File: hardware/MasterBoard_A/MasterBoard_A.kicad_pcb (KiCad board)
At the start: 2 copper layers, 60 x 100 mm, 175 parts, among them J101 Main Current Hall Sensor, J102 Global LV and CAN, J103 HRLV, J105 Conn_02x05_Odd_Even, J106 uart, J301 RJ45_Amphenol_RJMG1BD3B8K1ANR, K101 G5Q-1A 24Vdc, Q101 MMBT5550L, Q102 MMBT5550L, Q103 MMBT5550L, Q301 MMBT5550L, Q302 MMBT5550L, Q401 MMBT5550L, Q501 MMBT5550L, Q502 MMBT5550L, SW101 SW_Push, U101 MCP2542FDxMF, U102 MCP2542FDxMF, U104 MCP9700x-ETT, U105 XM0G3507QPTRQ1, U201 Si1450DH, U202 LM74502, U203 Si1450DH, U204 AP64060ZQ, U205 AP64060ZQ, U301 W5500, U401 MCP1501-40xSN, U402 TLV713185PDBV, U403 NSI5030, U404 MCP33151, U405 MCP33151, U406 MIC7300M5, U407 Si1450DH, U408 Si1450DH, U409 NCV68061, U501 NSI5030, U502 Si1450DH, U503 NCV68061, U504 MCP2542FDxMF, U505 AP7384-50SA, U506 ISOM8110, U507 ISOM8110, U508 STISO620, Y301 Crystal_GND24

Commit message: bucks and eyeballed layout
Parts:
- added C321: 220n, Capacitor_SMD:C_0805_2012Metric_Pad1.18x1.45mm_HandSolder, F.Cu at (136.6, 106.9)
- moved R209 69.5 mm to (176.3, 135.5), turned to 180 degrees
- moved R201 60.9 mm to (172.8, 120.9), turned to -90 degrees
- moved U204 60.7 mm to (179.1, 121.8), turned to 180 degrees
- moved C205 58.1 mm to (176.3, 130.7)
- moved C206 57.1 mm to (176.3, 133.0)
- moved C204 54.8 mm to (179.5, 124.8), turned to 180 degrees
- moved D203 54.5 mm to (180.6, 127.8)
- moved C207 53.7 mm to (180.9, 134.1), turned to 90 degrees
- moved R207 53.5 mm to (183.0, 134.2), turned to -90 degrees
- moved C203 51.9 mm to (179.6, 118.5)
- moved L201 47.7 mm to (175.4, 126.3), turned to 90 degrees
- moved D201 43.1 mm to (174.9, 121.5), turned to 90 degrees
- moved R208 38.9 mm to (183.2, 121.7), turned to -90 degrees
- moved R204 36.8 mm to (173.1, 101.0), turned to -90 degrees
- moved D202 33.9 mm to (175.1, 101.0), turned to 90 degrees
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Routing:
- net +3.3V: track 0.00 -> 95.5 mm, vias 0 -> 1
- net +5V: track 0.00 -> 25.2 mm
- net Net-(U204-FB): track 0.00 -> 15.9 mm
- net Net-(U205-FB): track 0.00 -> 15.6 mm
- net Net-(D203-K): track 0.00 -> 7.65 mm
- net Net-(D204-K): track 0.00 -> 7.38 mm
- net LV+: track 27.5 -> 33.4 mm
- net Net-(C213-Pad1): track 0.00 -> 3.35 mm
- net Net-(C207-Pad1): track 0.00 -> 3.19 mm
- net GND: track 18.0 -> 21.0 mm, vias 53 -> 72
- net Net-(D201-A): track 0.00 -> 2.57 mm
- net Net-(U205-BST): track 0.00 -> 2.25 mm
- net Net-(U204-BST): track 0.00 -> 2.14 mm
- net Net-(D202-A): track 0.00 -> 2.01 mm

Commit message: saturn tool kit my beloved
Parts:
- moved C506 58.6 mm to (188.2, 133.4), turned to 90 degrees
- moved U508 49.7 mm to (184.2, 141.0), turned to -90 degrees
- moved U502 45.9 mm to (150.0, 152.0), turned to 90 degrees
- moved Q501 45.4 mm to (137.0, 147.0), turned to -22.5 degrees
- moved U504 45.3 mm to (173.5, 149.1), turned to 180 degrees
- moved R506 44.2 mm to (142.6, 148.4), turned to -45 degrees
- moved R504 43.9 mm to (172.0, 152.8), turned to 180 degrees
- moved Q502 43.0 mm to (147.2, 147.6), turned to 180 degrees
- moved U506 42.4 mm to (133.0, 141.0)
- moved R505 42.1 mm to (168.4, 155.6), turned to 90 degrees
- moved R503 41.6 mm to (140.6, 145.4), turned to 180 degrees
- moved C505 40.9 mm to (179.2, 146.4), turned to -90 degrees
- moved U505 40.6 mm to (144.2, 156.8), turned to -90 degrees
- moved C501 40.5 mm to (151.2, 145.4), turned to 180 degrees
- moved C503 40.2 mm to (145.4, 152.0), turned to -90 degrees
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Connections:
- J103 pad 1: /HRLV_CAN- -> /HRLV_CAN+
- J103 pad 4: /HRLV_CAN+ -> /HRLV_CAN-
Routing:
- net /HRLV interface/+5V: track 0.00 -> 68.0 mm
- net +3.3V: track 95.5 -> 153.9 mm, vias 1 -> 5
- net /HRLV interface/LV+: track 0.00 -> 54.7 mm
- net /HRLV_LV+: track 0.00 -> 21.4 mm
- net Net-(U504-RXD): track 0.00 -> 10.8 mm
- net Net-(U504-TXD): track 0.00 -> 10.4 mm
- net /HRLV_IL+: track 0.00 -> 9.38 mm
- net /HRLV_CAN-: track 0.00 -> 9.17 mm
- net /HRLV_CAN+: track 0.00 -> 9.17 mm
- net Net-(D503-K): track 0.00 -> 7.49 mm
- net /HRLV_IL-: track 0.00 -> 6.94 mm
- net Net-(Q502-E): track 0.00 -> 5.89 mm
- net Net-(U506--TX): track 0.00 -> 5.83 mm
- net Net-(U502-G): track 0.00 -> 5.23 mm
- net Net-(U507--TX): track 0.00 -> 5.08 mm, vias 0 -> 2
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- added copper zone on B.Cu, net /HRLV_LV-
- added copper zone on F.Cu, net /HRLV_LV-

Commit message: mb layout: all but mcu bundle
thou who completes thy layout must endure excel
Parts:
- removed C103, C405, C407: 220n, Capacitor_SMD:C_0805_2012Metric_Pad1.18x1.45mm_HandSolder
- removed D401: 10V, Diode_SMD:D_0805_2012Metric_Pad1.15x1.40mm_HandSolder
- removed Q401: MMBT5550L, Package_TO_SOT_SMD:SOT-23
- removed R101, R103, R401, R504: 40.2k, Resistor_SMD:R_0805_2012Metric_Pad1.20x1.40mm_HandSolder
- removed R402, R403: 22.1k, Resistor_SMD:R_0805_2012Metric_Pad1.20x1.40mm_HandSolder
- removed U403: NSI5030, Diode_SMD:Nexperia_CFP3_SOD-123W
- removed U406: MIC7300M5, Package_TO_SOT_SMD:TSOT-23-5
- removed U407: Si1450DH, Package_TO_SOT_SMD:SOT-363_SC-70-6_Handsoldering
- moved U401 52.3 mm to (154.7, 124.8), turned to 180 degrees
- moved C401 43.9 mm to (156.6, 130.6), turned to 180 degrees
- moved C402 43.0 mm to (156.6, 128.6), turned to 180 degrees
- moved U402 42.6 mm to (156.7, 133.4), turned to 180 degrees
- moved U408 41.9 mm to (142.4, 133.3)
- moved U409 35.9 mm to (148.2, 133.3), turned to 180 degrees
- moved C406 35.4 mm to (152.7, 130.2), turned to -90 degrees
- moved U101 34.4 mm to (181.2, 120.2)
- moved J101 34.1 mm to (138.1, 130.0), turned to 90 degrees
- moved U405 32.7 mm to (147.6, 122.0), turned to 90 degrees
- moved U104 32.5 mm to (207.5, 96.4)
- moved C408 29.5 mm to (148.1, 130.0)
- moved C409 29.3 mm to (148.1, 127.0)
- moved U102 29.0 mm to (186.6, 127.1), turned to 90 degrees
- moved C404 28.7 mm to (141.3, 120.2), turned to 90 degrees
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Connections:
- C410 pad 1: /Main Current Hall Sensing/Vreg -> +5V
- J102 pad 3: /G_CAN_+ -> /G_CAN-
- J102 pad 6: /G_CAN_- -> /G_CAN+
- U101 pad 8: Net-(U101-STBY) -> GND
- U102 pad 8: Net-(U102-STBY) -> GND
- U402 pad 3: Net-(U402-EN) -> +5V
- U408 pad 4: /Main Current Hall Sensing/Vreg -> +5V
- U409 pad 3: /Main Current Hall Sensing/Vreg -> +5V
- U409 pad 6: /Main Current Hall Sensing/Vreg -> +5V
- U504 pad 8: Net-(U504-STBY) -> /HRLV_LV-
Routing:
- net +5V: track 25.2 -> 123.7 mm
- net /G_CAN+: track 0.00 -> 67.4 mm, vias 0 -> 2
- net /G_CAN-: track 0.00 -> 67.4 mm, vias 0 -> 2
- net LV+: track 33.4 -> 80.2 mm
- net +3.3V: track 153.9 -> 191.5 mm
- net /Main Current Hall Sensing/4.096Vref: track 0.00 -> 25.3 mm
- net /Main Current Hall Sensing/1.8VA: track 0.00 -> 23.6 mm, vias 0 -> 2
- net /MCHall_5Vin: track 0.00 -> 12.7 mm
- net /HRLV interface/CAN_RX: track 0.00 -> 10.9 mm
- net Net-(U404-Ain+): track 0.00 -> 10.2 mm
- net /HRLV interface/CAN_TX: track 0.00 -> 8.19 mm
- net /mchs.MISO/POCI: track 0.00 -> 6.89 mm
- net Net-(U408-G): track 0.00 -> 6.30 mm, vias 0 -> 2
- net /mchs.SCLK: track 0.00 -> 5.99 mm, vias 0 -> 2
- net Net-(U405-Ain+): track 0.00 -> 4.87 mm
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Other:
- board text added: "trust me bro, length tuning can to mm match is essential"

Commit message: mb ready for review
one of yall poor souls has to verify the schematic and layout
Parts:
- removed C106: 220n, Capacitor_SMD:C_0805_2012Metric_Pad1.18x1.45mm_HandSolder
- removed SW101: SW_Push, Button_Switch_SMD:SW_SPST_PTS645
- removed TP101: TestPoint, TestPoint:TestPoint_THTPad_3.0x3.0mm_Drill1.5mm
- removed TP102, TP103, TP104: TestPoint, TestPoint:TestPoint_Loop_D2.50mm_Drill1.0mm_LowProfile
- removed U104: MCP9700x-ETT, Package_TO_SOT_SMD:SOT-23-3
- added C208: 220n, Capacitor_SMD:C_0805_2012Metric_Pad1.18x1.45mm_HandSolder, F.Cu at (156.9, 136.8)
- added R1: 100, Resistor_SMD:R_1206_3216Metric_Pad1.30x1.75mm_HandSolder, F.Cu at (145.7, 114.6)
- added R2: 100, Resistor_SMD:R_1206_3216Metric_Pad1.30x1.75mm_HandSolder, F.Cu at (147.9, 114.6)
- added R311: 4.99k, Resistor_SMD:R_1206_3216Metric_Pad1.30x1.75mm_HandSolder, F.Cu at (134.9, 110.3)
- added R312: 4.99k, Resistor_SMD:R_1206_3216Metric_Pad1.30x1.75mm_HandSolder, F.Cu at (134.9, 112.6)
- C313: value 100n -> 220n; footprint Capacitor_SMD:C_0603_1608Metric_Pad1.08x0.95mm_HandSolder -> Capacitor_SMD:C_0805_2012Metric_Pad1.18x1.45mm_HandSolder
- moved J106 86.0 mm to (135.4, 121.0), turned to 180 degrees
- moved C107 84.7 mm to (143.3, 114.6), turned to -90 degrees
- moved J105 79.1 mm to (152.8, 110.5), turned to -90 degrees
- moved R111 61.2 mm to (172.2, 108.5), turned to 180 degrees
- moved U105 56.1 mm to (162.7, 110.0), turned to 180 degrees
- moved D106 54.3 mm to (168.8, 120.4), turned to 180 degrees
- moved D104 53.7 mm to (168.8, 118.5), turned to 180 degrees
- moved D103 53.7 mm to (173.4, 98.8), turned to -90 degrees
- moved D105 53.7 mm to (172.8, 106.4)
- moved R109 42.6 mm to (172.8, 104.5), turned to 180 degrees
- moved C321 42.3 mm to (155.4, 69.0)
- moved R112 41.2 mm to (172.7, 112.6)
- moved R107 40.0 mm to (172.8, 102.6), turned to 180 degrees
- moved C109 37.2 mm to (172.7, 110.7)
- moved C110 36.6 mm to (172.7, 114.6)
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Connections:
- net Net-(U105-VCORE) renamed /vcore
- C313 pad 1: /Ethernet/+3.3VA -> +3.3V
- D103 pad 1: Net-(D103-K) -> GND
- D103 pad 2: /led.i2 -> Net-(D103-A)
- D105 pad 1: Net-(D105-K) -> GND
- D105 pad 2: /led.BMSFault -> Net-(D105-A)
- R107 pad 1: Net-(D103-K) -> Net-(D103-A)
- R107 pad 2: GND -> /led.i2
- R109 pad 1: Net-(D105-K) -> Net-(D105-A)
- R109 pad 2: GND -> /led.BMSFault
- U105 pad 11: unconnected-(U105-PA5_HFXIN_FCC_IN-Pad11) -> /led.BMSFault
- U105 pad 12: unconnected-(U105-PA6_HFCLK_IN_HFXOUT-Pad12) -> /led.i2
- U105 pad 21: unconnected-(U105-PB7-Pad21) -> /IL.sense
- U105 pad 22: unconnected-(U105-PB8-Pad22) -> /IL.forward
- U105 pad 23: unconnected-(U105-PB9-Pad23) -> GND
- U105 pad 24: unconnected-(U105-PB14-Pad24) -> /eth.reset_N
- U105 pad 25: unconnected-(U105-PB15-Pad25) -> /eth.irq_N
- U105 pad 27: unconnected-(U105-PA12_FCC_IN-Pad27) -> /eth.SCLK
- U105 pad 28: unconnected-(U105-PA13-Pad28) -> /eth.MISO/POCI
- U105 pad 29: unconnected-(U105-PA14_CLK_OUT_A0_12-Pad29) -> /eth.MOSI/PICO
- U105 pad 30: unconnected-(U105-PA15_A1_0-Pad30) -> /eth.cs_N
- U105 pad 31: unconnected-(U105-PA16_A1_1_FCC_IN-Pad31) -> /mchs.MISO/POCI
- U105 pad 32: unconnected-(U105-PA17_A1_2-Pad32) -> /mchs.SCLK
- U105 pad 33: unconnected-(U105-PA18_A1_3-Pad33) -> /mchs.MOSI/PICO
- U105 pad 34: unconnected-(U105-PA19_SWDIO-Pad34) -> /prog.SWDIO
- U105 pad 35: unconnected-(U105-PA20_SWCLK-Pad35) -> /prog.SWCLK
- U105 pad 36: unconnected-(U105-PB17_A1_4-Pad36) -> +3.3V
- U105 pad 37: unconnected-(U105-PB18_A1_5-Pad37) -> /mchs.cs_per
- U105 pad 38: unconnected-(U105-PB19_A1_6-Pad38) -> /mchs.cs_imp
- U105 pad 39: unconnected-(U105-PA21_A1_7_VREF--Pad39) -> /prog.uart_ui_tx
- U105 pad 40: unconnected-(U105-PA22_CLK_OUT_A0_7-Pad40) -> /prog.uart_ui_rx
- U105 pad 41: unconnected-(U105-PB20_A0_6-Pad41) -> /hrlv.pres_hrlv
- U105 pad 42: unconnected-(U105-PB24_A0_5-Pad42) -> /hrlv.pres_interlock
- U105 pad 43: unconnected-(U105-PA23_VREF+-Pad43) -> /led.sched
- U105 pad 44: unconnected-(U105-PA24_A0_3-Pad44) -> /led.i1
- U105 pad 46: unconnected-(U105-PA26_A0_1-Pad46) -> /can.tx
- U105 pad 47: unconnected-(U105-PA27_RTC_OUT_A0_0-Pad47) -> /can.rx
- U105 pad 5: unconnected-(U105-PA31_CLK_OUT-Pad5) -> +3.3V
- U301 pad 25: Net-(Q301-B) -> Net-(U301-LINKLED)
- U301 pad 27: Net-(Q302-B) -> Net-(U301-ACTLED)
- U404 pad 7: /mchs.MISO/POCI -> /Main Current Hall Sensing/SDO
- U404 pad 8: /mchs.SCLK -> /Main Current Hall Sensing/SCLK
- U405 pad 7: /mchs.MISO/POCI -> /Main Current Hall Sensing/SDO
- U405 pad 8: /mchs.SCLK -> /Main Current Hall Sensing/SCLK
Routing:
- net +3.3V: track 191.5 -> 299.9 mm, vias 5 -> 8
- net /hrlv.pres_hrlv: track 0.00 -> 48.1 mm, vias 0 -> 2
- net /IL.forward: track 0.00 -> 47.6 mm
- net /hrlv.pres_interlock: track 1.20 -> 37.3 mm, vias 0 -> 2
- net /prog.uart_ui_rx: track 0.00 -> 28.9 mm, vias 0 -> 2
- net /prog.uart_ui_tx: track 0.00 -> 27.9 mm, vias 0 -> 2
- net /can.rx: track 0.00 -> 23.0 mm
- net /eth.MOSI/PICO: track 0.00 -> 20.2 mm, vias 0 -> 2
- net /Main Current Hall Sensing/SCLK: track 0.00 -> 19.4 mm
- net /mchs.cs_per: track 0.00 -> 19.3 mm, vias 0 -> 2
- net /mchs.cs_imp: track 0.00 -> 18.7 mm, vias 0 -> 2
- net /eth.cs_N: track 0.00 -> 18.5 mm
- net Net-(Q301-B): track 45.3 -> 26.9 mm
- net /eth.MISO/POCI: track 0.00 -> 18.2 mm, vias 0 -> 2
- net /eth.SCLK: track 0.00 -> 17.5 mm
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- added copper zone on F.Cu, net +3.3V
- added copper zone on F.Cu, net /vcore
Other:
- outline, holes or cut-outs redrawn
- board text added: "100MB/S ethernet"
- board text added: "5V out"
- board text added: "Big Hall Sensor"
- board text added: "CAN+"
- board text added: "CAN-"
- board text added: "GLV+ (9,34)V"
- board text added: "GLV-"
- board text added: "GND"
- board text added: "HRLV interface"
- board text added: "IL return"
- board text added: "IL_A"
- board text added: "IL_B"
- board text added: "LV+ (5.5 , 35)V"
- board text added: "LV-"
- board text added: "Master Board A 1.1 (testing use only) github.com/Gregification/BeeMS/ 1/13/2025 - pinning & hardware info: {dblquote}/hardware/MasterBoard_A/meta.xlsx{dblquote} - software: {dblquote}/MB_MSPM0G3507_A{dblquote} - no hardware watchdog - no PWM bank"
- board text added: "RX"
- board text added: "TX"
- board text added: "bms fault"
- board text added: "impercise"
- board text added: "indicator 1"
- board text added: "indicator 2"
- board text added: "percise"
- board text added: "scheduler"
- board text added: "tty 115200 8N1"
- board text added: "we dont talk about this routing"
- board text removed: "CAN bus"
- board text removed: "JLCJLCJLCJLC"
- board text removed: "Master Board A 1.0 (testing use only) github.com/Gregification/BeeMS/ 12/24/2025 - pinning & hardware info: {dblquote}/hardware/MasterBoard_A/meta.xlsx{dblquote} - software: {dblquote}/MB_MSPM0G3507_A{dblquote} - no hardware watchdog - reduced pwm bank. POC."
- board text removed: "TSBP internal LV interface"
- board text removed: "ethernet"
- board text removed: "fuse >0.4A"
- board text removed: "fuse >0.8A"
- board text removed: "interlock"
- board text removed: "pwm bank 1"

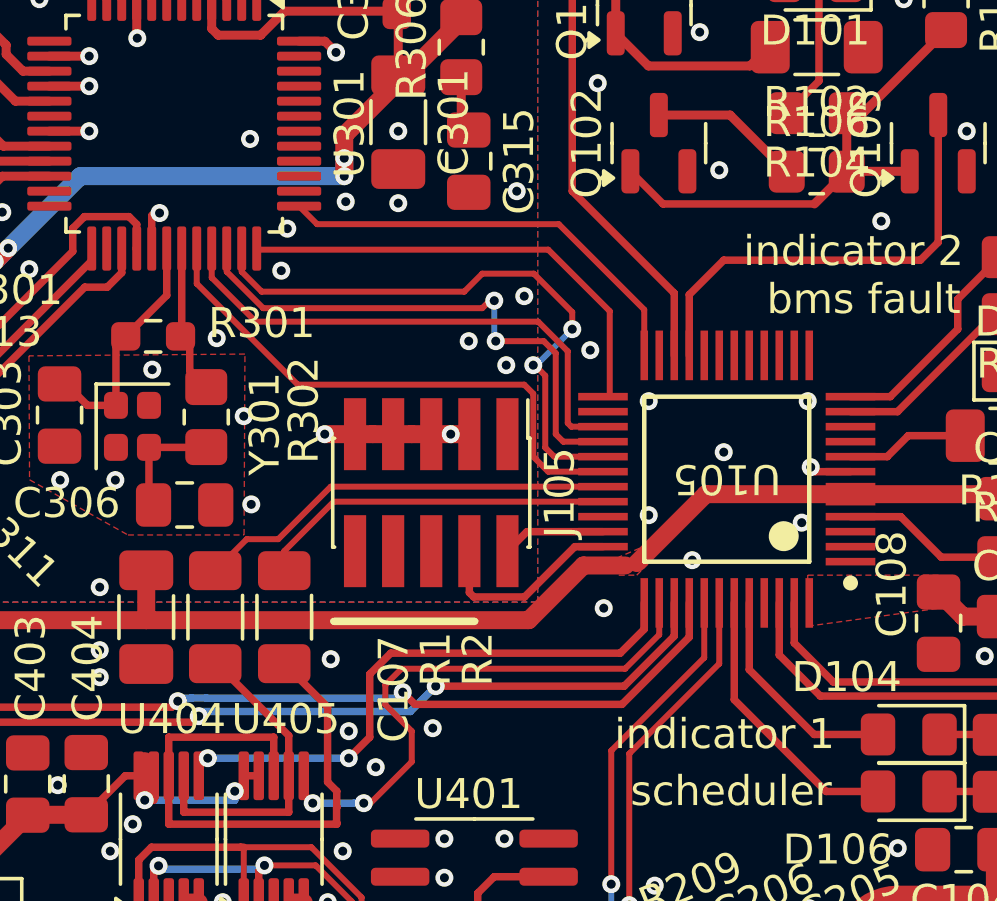
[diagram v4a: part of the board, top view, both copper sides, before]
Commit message: master board shuffling
jlc says $2. yippie
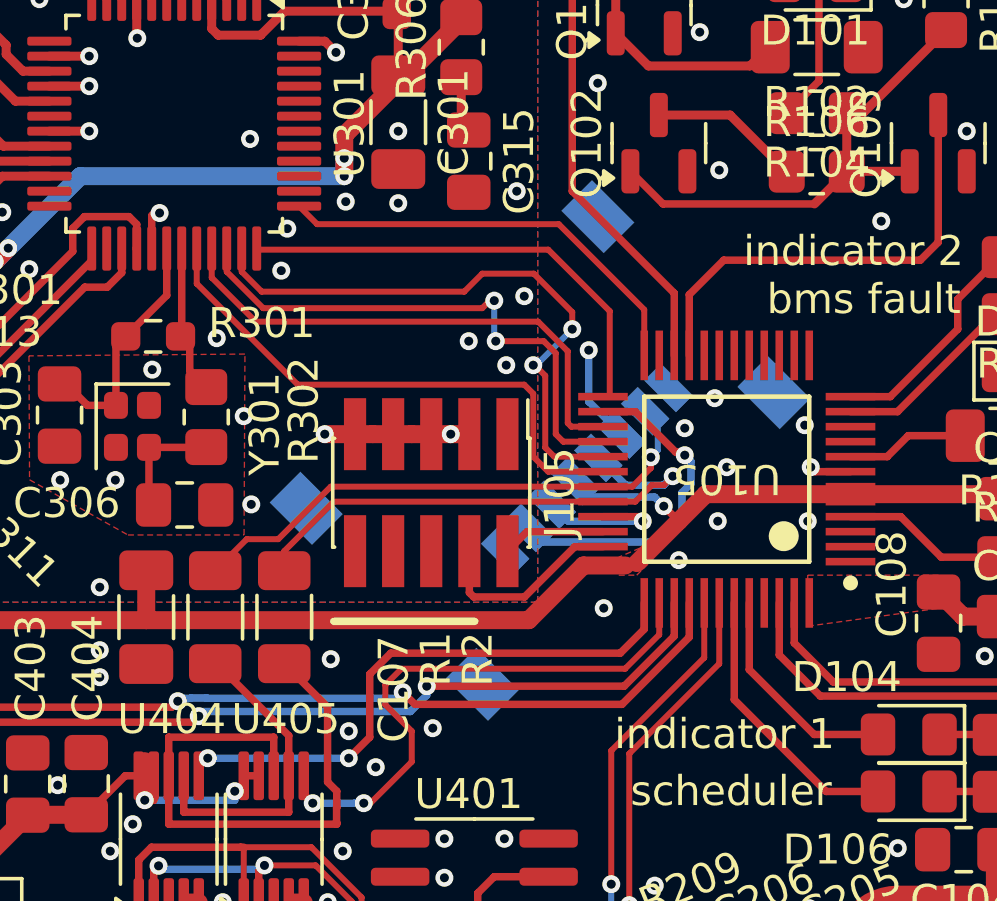
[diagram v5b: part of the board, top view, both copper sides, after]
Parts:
- added J107: Micro_SD_Card, Connector_Card:microSD_HC_Wuerth_693072010801, B.Cu at (156.5, 109.0)
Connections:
- U105 pad 26: unconnected-(U105-PB16-Pad26) -> /mchs.cs_sd
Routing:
- net /mchs.cs_sd: track 0.00 -> 11.2 mm, vias 0 -> 1
- net /mchs.SCLK: track 12.0 -> 17.6 mm, vias 0 -> 1
- net /mchs.MOSI/PICO: track 0.00 -> 4.65 mm, vias 0 -> 1
- net /mchs.MISO/POCI: track 14.1 -> 18.1 mm, vias 0 -> 1
- net +3.3V: track 299.9 -> 303.9 mm, vias 8 -> 9
- net GND: track 27.3 -> 30.6 mm, vias 179 -> 180

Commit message: me when i forget a wire
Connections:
- J106 pad 2: /prog.uart_ui_tx -> /prog.uart_ui_rx
- J106 pad 3: /prog.uart_ui_rx -> /prog.uart_ui_tx
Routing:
- net GND: track 30.6 -> 36.1 mm, vias 180 -> 193
- net Net-(U201-G): track 20.3 -> 22.0 mm
- net /Main Current Hall Sensing/SCLK: track 19.4 -> 18.7 mm
- net +5V: track 123.8 -> 124.4 mm
- net /GLV PSU/GLV+: track 40.5 -> 41.2 mm
- net Net-(U205-FB): track 15.6 -> 16.2 mm
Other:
- board text added: "600Vdc galv ISO"
- board text added: "fuse ~800mA"
- board text added: "ground loop from LV bulk to diode crosses sense line"
- board text added: "hope and dreams kind of wiring"
- board text removed: "Big Hall Sensor"
